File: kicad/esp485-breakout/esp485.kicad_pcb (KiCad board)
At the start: 2 copper layers, 25.4 x 25.4 mm, 21 parts, among them J1 Conn_01x08, J2 Conn_01x08, SW1 SW_Push, SW2 SW_Push, U1 MAX3485, U2 ESP-WROOM-02, U3 AMS1117-3.3

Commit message: font size adjusted
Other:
- board text added: "."
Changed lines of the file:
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@@
   (general
     (thickness 1.6)
-    (drawings 26)
+    (drawings 27)
     (tracks 182)
     (zones 0)
@@
   (layers
     (0 F.Cu signal hide)
-    (31 B.Cu signal)
+    (31 B.Cu signal hide)
     (32 B.Adhes user)
     (33 F.Adhes user)
@@
     (tags "CMS SOT")
     (attr smd)
-    (fp_text reference U3 (at 0.127 0.381 180) (layer B.SilkS)
+    (fp_text reference U3 (at 2.794 3.175 180) (layer B.SilkS)
       (effects (font (size 1 1) (thickness 0.15)) (justify mirror))
     )
@@
     (tags "resistor handsolder")
     (attr smd)
-    (fp_text reference R2 (at -0.254 -1.143) (layer B.SilkS)
-      (effects (font (size 1 1) (thickness 0.15)) (justify mirror))
+    (fp_text reference R2 (at 0 1.143) (layer B.SilkS)
+      (effects (font (size 0.8 0.8) (thickness 0.14)) (justify mirror))
     )
     (fp_text value 10K (at 0 -1.43) (layer B.Fab)
@@
     (tags "resistor handsolder")
     (attr smd)
-    (fp_text reference R3 (at 0.127 -1.143) (layer B.SilkS)
-      (effects (font (size 1 1) (thickness 0.15)) (justify mirror))
+    (fp_text reference R3 (at 0 1.143) (layer B.SilkS)
+      (effects (font (size 0.8 0.8) (thickness 0.14)) (justify mirror))
     )
     (fp_text value 10K (at 0 -1.43) (layer B.Fab)
@@
     (attr smd)
     (fp_text reference R7 (at 0 1.27) (layer B.SilkS)
-      (effects (font (size 1 1) (thickness 0.15)) (justify mirror))
+      (effects (font (size 0.8 0.8) (thickness 0.14)) (justify mirror))
     )
     (fp_text value 10K (at 0 -1.43) (layer B.Fab)
@@
     (attr smd)
     (fp_text reference R8 (at 0 1.016) (layer B.SilkS)
-      (effects (font (size 1 1) (thickness 0.15)) (justify mirror))
+      (effects (font (size 0.8 0.8) (thickness 0.14)) (justify mirror))
     )
     (fp_text value 10K (at 0 -1.43) (layer B.Fab)
@@
     (tags "resistor handsolder")
     (attr smd)
-    (fp_text reference R9 (at -0.381 -1.016) (layer B.SilkS)
-      (effects (font (size 1 1) (thickness 0.15)) (justify mirror))
+    (fp_text reference R9 (at 0 1.143) (layer B.SilkS)
+      (effects (font (size 0.8 0.8) (thickness 0.14)) (justify mirror))
     )
     (fp_text value 10K (at 0 -1.43) (layer B.Fab)
@@
     )
   )
+  (gr_text . (at 145.161 108.839) (layer B.SilkS)
+    (effects (font (size 1.5 1.5) (thickness 0.3)) (justify mirror))
+  )
   (gr_text IO0 (at 131.445 109.22 -90) (layer B.SilkS)

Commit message: esp485-12f added
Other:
- board text added: "+"
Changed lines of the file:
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@@
   (general
     (thickness 1.6)
-    (drawings 27)
+    (drawings 29)
     (tracks 182)
     (zones 0)
@@
     (46 B.CrtYd user)
     (47 F.CrtYd user)
-    (48 B.Fab user hide)
+    (48 B.Fab user)
     (49 F.Fab user)
   )
@@
     (tags "capacitor handsolder")
     (attr smd)
-    (fp_text reference C5 (at -2.54 0 180) (layer B.SilkS)
+    (fp_text reference C5 (at -2.54 0.254 180) (layer B.SilkS)
       (effects (font (size 1 1) (thickness 0.15)) (justify mirror))
     )
@@
     )
   )
+  (gr_text + (at 143.256 98.933) (layer B.SilkS)
+    (effects (font (size 0.8 0.8) (thickness 0.2)) (justify mirror))
+  )
+  (gr_text + (at 143.256 96.266) (layer B.SilkS)
+    (effects (font (size 0.8 0.8) (thickness 0.2)) (justify mirror))
+  )
   (gr_text . (at 145.161 108.839) (layer B.SilkS)

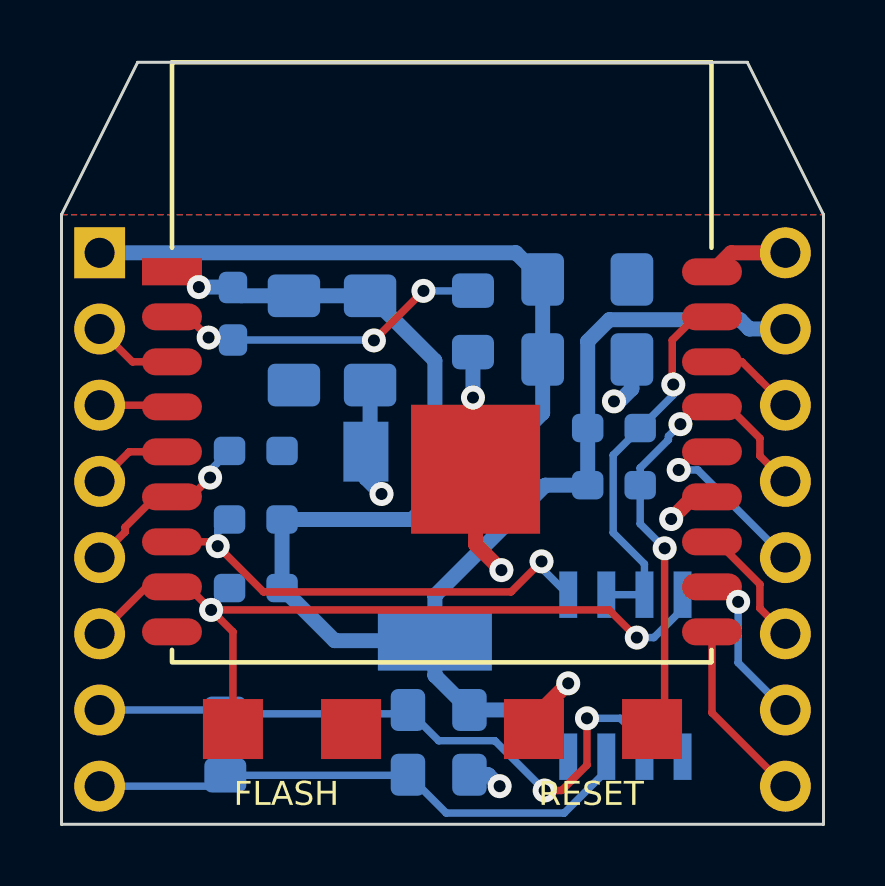
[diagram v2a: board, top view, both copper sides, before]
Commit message: add vias to enlarge gnd pad
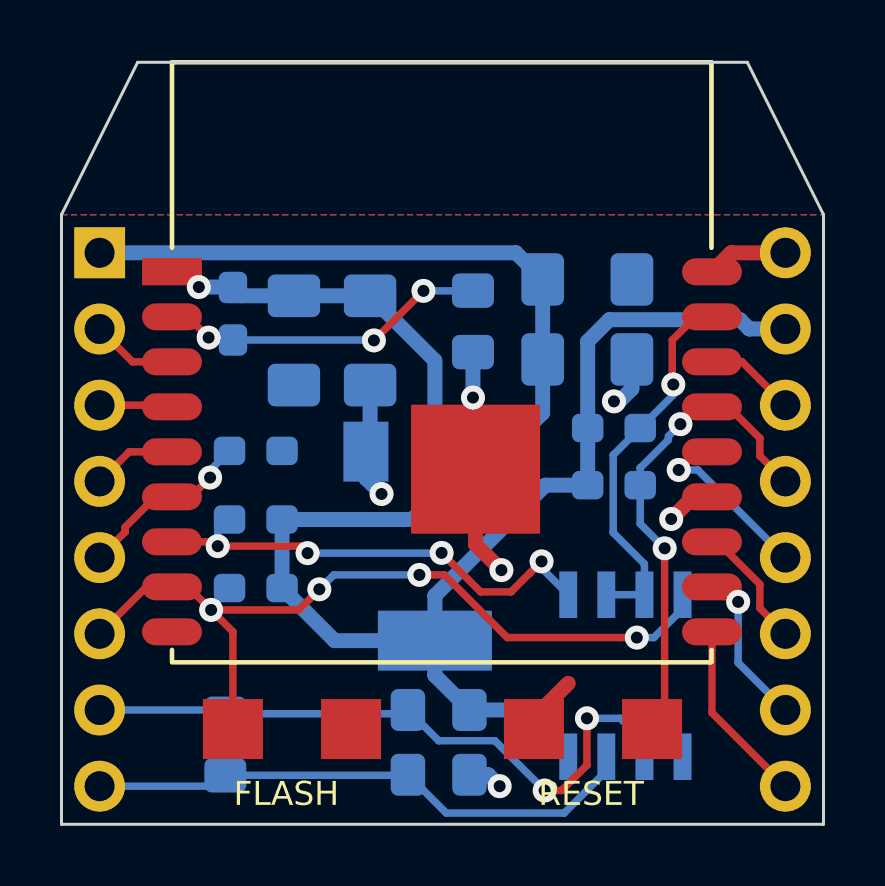
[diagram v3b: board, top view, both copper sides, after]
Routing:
- net Net-(J1-Pad6): track 26.9 -> 27.9 mm, vias 2 -> 4
- net Net-(R2-Pad1): vias 2 -> 4
- net GND: vias 7 -> 6
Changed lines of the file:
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@@
     (thickness 1.6)
     (drawings 29)
-    (tracks 182)
+    (tracks 196)
     (zones 0)
     (modules 21)
@@
   (page A4)
   (layers
-    (0 F.Cu signal hide)
-    (31 B.Cu signal hide)
+    (0 F.Cu signal)
+    (31 B.Cu signal)
     (32 B.Adhes user)
     (33 F.Adhes user)
@@
   (segment (start 133.257414 108.424685) (end 133.257414 108.310586) (width 0.25) (layer B.Cu) (net 2))
   (via (at 147.447 109.347) (size 0.8) (drill 0.4) (layers F.Cu B.Cu) (net 2))
-  (segment (start 133.257414 108.424685) (end 146.524685 108.424685) (width 0.25) (layer F.Cu) (net 2))
-  (segment (start 146.524685 108.424685) (end 147.447 109.347) (width 0.25) (layer F.Cu) (net 2))
+  (segment (start 147.447 109.347) (end 148.016 109.347) (width 0.25) (layer B.Cu) (net 2))
+  (segment (start 148.016 109.347) (end 148.971 108.392) (width 0.25) (layer B.Cu) (net 2) (status 20))
   (segment (start 148.971 108.392) (end 148.971 107.917) (width 0.25) (layer B.Cu) (net 2) (status 30))
-  (segment (start 148.016 109.347) (end 148.971 108.392) (width 0.25) (layer B.Cu) (net 2) (status 20))
-  (segment (start 147.447 109.347) (end 148.016 109.347) (width 0.25) (layer B.Cu) (net 2))
   (segment (start 133.985 109.152271) (end 133.985 112.395) (width 0.25) (layer F.Cu) (net 2) (status 20))
   (segment (start 133.257414 108.424685) (end 133.985 109.152271) (width 0.25) (layer F.Cu) (net 2))
+  (via (at 136.865041 107.736959) (size 0.8) (drill 0.4) (layers F.Cu B.Cu) (net 2))
+  (segment (start 133.257414 108.424685) (end 136.177315 108.424685) (width 0.25) (layer F.Cu) (net 2))
+  (segment (start 136.177315 108.424685) (end 136.865041 107.736959) (width 0.25) (layer F.Cu) (net 2))
+  (via (at 140.199828 107.256976) (size 0.8) (drill 0.4) (layers F.Cu B.Cu) (net 2))
+  (segment (start 136.865041 107.736959) (end 137.345024 107.256976) (width 0.25) (layer B.Cu) (net 2))
+  (segment (start 137.345024 107.256976) (end 140.199828 107.256976) (width 0.25) (layer B.Cu) (net 2))
+  (segment (start 146.881315 109.347) (end 147.447 109.347) (width 0.25) (layer F.Cu) (net 2))
+  (segment (start 143.12759 109.347) (end 146.881315 109.347) (width 0.25) (layer F.Cu) (net 2))
+  (segment (start 141.037566 107.256976) (end 143.12759 109.347) (width 0.25) (layer F.Cu) (net 2))
+  (segment (start 140.199828 107.256976) (end 141.037566 107.256976) (width 0.25) (layer F.Cu) (net 2))
   (segment (start 131.403 104.655) (end 131.953 104.655) (width 0.25) (layer F.Cu) (net 3) (status 30))
   (segment (start 130.389999 105.668001) (end 131.403 104.655) (width 0.25) (layer F.Cu) (net 3) (status 20))
@@
   (segment (start 149.953 104.655) (end 149.333162 104.655) (width 0.5) (layer F.Cu) (net 6) (status 30))
   (segment (start 149.333162 104.655) (end 148.593404 105.394758) (width 0.5) (layer F.Cu) (net 6) (status 10))
-  (via (at 141.986 101.346) (size 0.8) (drill 0.4) (layers F.Cu B.Cu) (net 6))
   (segment (start 141.986 99.831) (end 141.986 101.346) (width 0.5) (layer B.Cu) (net 6) (status 10))
   (segment (start 138.557 103.008) (end 138.416 103.149) (width 0.5) (layer B.Cu) (net 6) (status 30))
   (segment (start 138.557 100.9285) (end 138.557 103.008) (width 0.5) (layer B.Cu) (net 6) (status 30))
-  (via (at 138.938 104.56) (size 0.8) (drill 0.4) (layers F.Cu B.Cu) (net 6))
   (segment (start 138.416 103.149) (end 138.416 104.038) (width 0.5) (layer B.Cu) (net 6) (status 30))
   (segment (start 138.416 104.038) (end 138.938 104.56) (width 0.5) (layer B.Cu) (net 6) (status 10))
-  (via (at 142.875 114.3) (size 0.8) (drill 0.4) (layers F.Cu B.Cu) (net 6))
   (segment (start 141.868 113.919) (end 142.494 113.919) (width 0.5) (layer B.Cu) (net 6) (status 10))
   (segment (start 142.494 113.919) (end 142.875 114.3) (width 0.5) (layer B.Cu) (net 6))
-  (via (at 145.161 110.871) (size 0.8) (drill 0.4) (layers F.Cu B.Cu) (net 6))
   (segment (start 144.018 112.395) (end 144.018 112.014) (width 0.5) (layer F.Cu) (net 6) (status 30))
   (segment (start 144.018 112.014) (end 145.161 110.871) (width 0.5) (layer F.Cu) (net 6) (status 10))
@@
   (segment (start 147.2835 101.051) (end 146.8615 101.473) (width 0.5) (layer B.Cu) (net 6))
   (segment (start 146.8615 101.473) (end 146.685 101.473) (width 0.5) (layer B.Cu) (net 6))
+  (segment (start 147.2835 100.076) (end 147.2835 101.051) (width 0.5) (layer B.Cu) (net 6) (status 10))
+  (via (at 138.938 104.56) (size 0.8) (drill 0.4) (layers F.Cu B.Cu) (net 6))
+  (via (at 141.986 101.346) (size 0.8) (drill 0.4) (layers F.Cu B.Cu) (net 6))
   (via (at 146.685 101.473) (size 0.8) (drill 0.4) (layers F.Cu B.Cu) (net 6))
-  (segment (start 147.2835 100.076) (end 147.2835 101.051) (width 0.5) (layer B.Cu) (net 6) (status 10))
+  (via (at 142.875 114.3) (size 0.8) (drill 0.4) (layers F.Cu B.Cu) (net 6))
   (segment (start 140.716 103.149) (end 140.716 100.1125) (width 0.5) (layer B.Cu) (net 7) (status 10))
   (segment (start 138.557 97.9535) (end 136.017 97.9535) (width 0.5) (layer B.Cu) (net 7) (status 30))
@@
   (segment (start 133.477 106.299) (end 133.477 105.805) (width 0.25) (layer B.Cu) (net 13) (status 20))
   (via (at 144.272 106.807) (size 0.8) (drill 0.4) (layers F.Cu B.Cu) (net 13))
+  (segment (start 144.272 106.807) (end 144.272 107.028) (width 0.25) (layer B.Cu) (net 13))
   (segment (start 144.272 107.028) (end 145.161 107.917) (width 0.25) (layer B.Cu) (net 13) (status 20))
-  (segment (start 144.272 106.807) (end 144.272 107.028) (width 0.25) (layer B.Cu) (net 13))
-  (segment (start 143.256 107.823) (end 144.272 106.807) (width 0.25) (layer F.Cu) (net 13))
-  (segment (start 133.477 106.299) (end 135.001 107.823) (width 0.25) (layer F.Cu) (net 13))
-  (segment (start 135.001 107.823) (end 143.256 107.823) (width 0.25) (layer F.Cu) (net 13))
+  (via (at 136.472 106.531976) (size 0.8) (drill 0.4) (layers F.Cu B.Cu) (net 13))
+  (segment (start 133.477 106.299) (end 136.239024 106.299) (width 0.25) (layer F.Cu) (net 13))
+  (segment (start 136.239024 106.299) (end 136.472 106.531976) (width 0.25) (layer F.Cu) (net 13))
+  (via (at 140.939959 106.522959) (size 0.8) (drill 0.4) (layers F.Cu B.Cu) (net 13))
+  (segment (start 136.472 106.531976) (end 140.930942 106.531976) (width 0.25) (layer B.Cu) (net 13))
+  (segment (start 140.930942 106.531976) (end 140.939959 106.522959) (width 0.25) (layer B.Cu) (net 13))
+  (segment (start 143.872001 107.206999) (end 144.272 106.807) (width 0.25) (layer F.Cu) (net 13))
+  (segment (start 142.240001 107.823001) (end 143.255999 107.823001) (width 0.25) (layer F.Cu) (net 13))
+  (segment (start 143.255999 107.823001) (end 143.872001 107.206999) (width 0.25) (layer F.Cu) (net 13))
+  (segment (start 140.939959 106.522959) (end 142.240001 107.823001) (width 0.25) (layer F.Cu) (net 13))
   (segment (start 130.635 100.155) (end 131.953 100.155) (width 0.25) (layer F.Cu) (net 14) (status 20))
   (segment (start 129.54 99.06) (end 130.635 100.155) (width 0.25) (layer F.Cu) (net 14) (status 10))

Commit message: migrated to single wire half duplex method
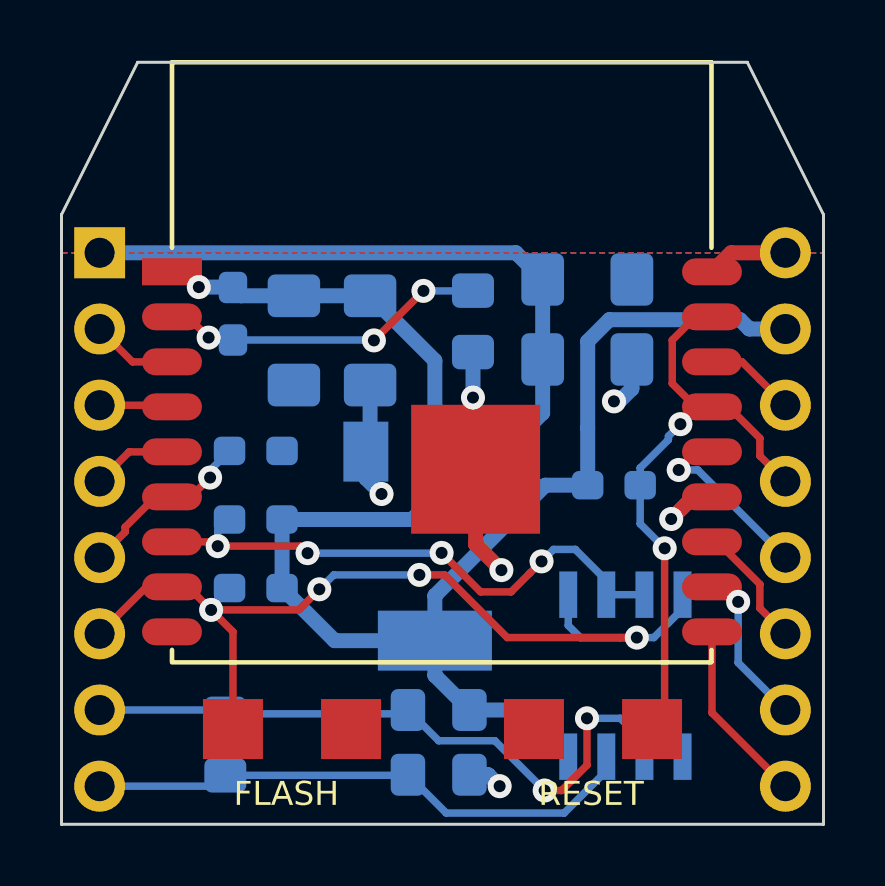
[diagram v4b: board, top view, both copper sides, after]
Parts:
- removed R8: 10K, Resistor_SMD:R_0603_1608Metric_Pad1.05x0.95mm_HandSolder
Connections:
- net Net-(J1-Pad2) renamed /IO14
- net Net-(J1-Pad3) renamed /IO12
- net Net-(J1-Pad4) renamed /IO13
- net Net-(J1-Pad5) renamed /IO15
- net Net-(J1-Pad7) renamed /A
- net Net-(J1-Pad8) renamed /B
- net Net-(J2-Pad3) renamed /TOUT
- net Net-(J2-Pad5) renamed /IO5
- net Net-(J2-Pad6) renamed /TXD
- net Net-(J2-Pad7) renamed /RXD
- net Net-(J2-Pad8) renamed /IO4
- J1 pad 6: Net-(J1-Pad6) -> /IO0
- J2 pad 4: Net-(J2-Pad4) -> /RST
- R3 pad 1: Net-(J1-Pad6) -> /IO0
- R7 pad 2: Net-(J2-Pad4) -> /RST
- SW1 pad 1: Net-(J1-Pad6) -> /IO0
- SW2 pad 1: Net-(J2-Pad4) -> /RST
- U1 pad 1: Net-(R2-Pad1) -> /IO0
- U1 pad 2: Net-(R8-Pad2) -> Net-(R2-Pad1)
- U1 pad 3: Net-(R8-Pad2) -> Net-(R2-Pad1)
- U1 pad 4: Net-(J1-Pad6) -> /IO0
- U2 pad 15: Net-(J2-Pad4) -> /RST
- U2 pad 17: Net-(R8-Pad2) -> /RST
- U2 pad 8: Net-(J1-Pad6) -> /IO0
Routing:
- net /IO0: track 0.00 -> 31.4 mm, vias 0 -> 4
- net Net-(J1-Pad6): track 27.9 -> 0.00 mm, vias 4 -> 0
- net /RST: track 0.00 -> 21.1 mm, vias 0 -> 2
- net Net-(J2-Pad4): track 16.3 -> 0.00 mm, vias 2 -> 0
- net Net-(R8-Pad2): track 12.7 -> 0.00 mm, vias 1 -> 0
- net Net-(R2-Pad1): track 16.0 -> 19.2 mm
- net GND: track 18.4 -> 16.8 mm

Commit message: added 4 layers pcb
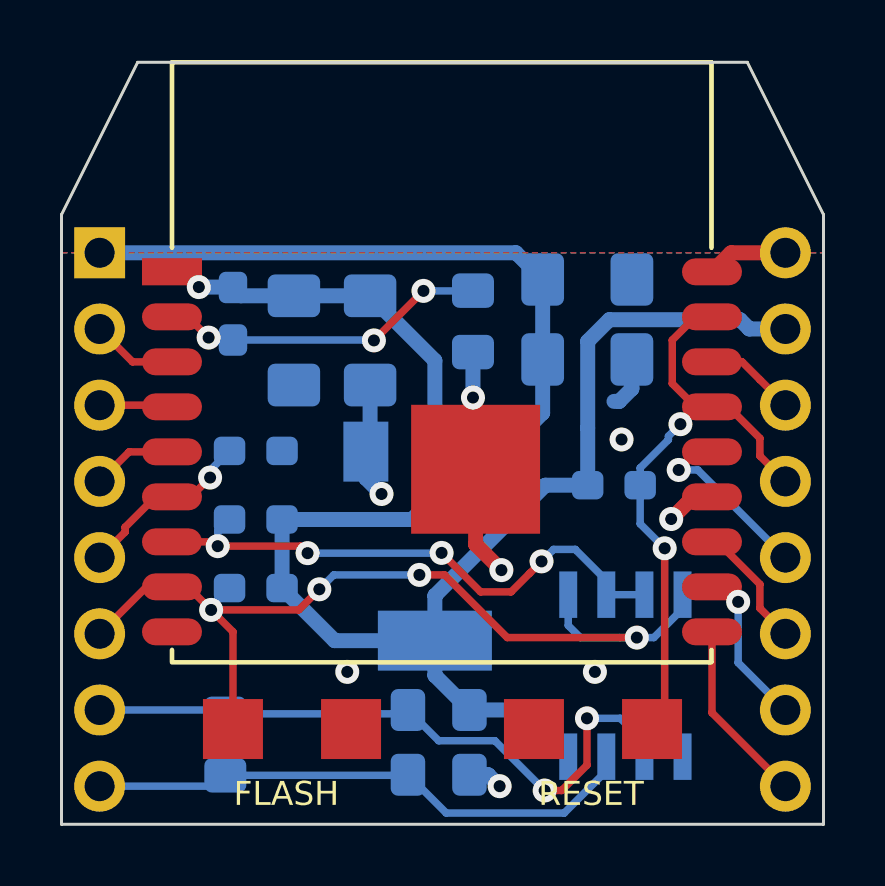
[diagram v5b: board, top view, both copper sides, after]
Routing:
- net GND: vias 6 -> 8

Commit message: put resistor between IO16 and RESET
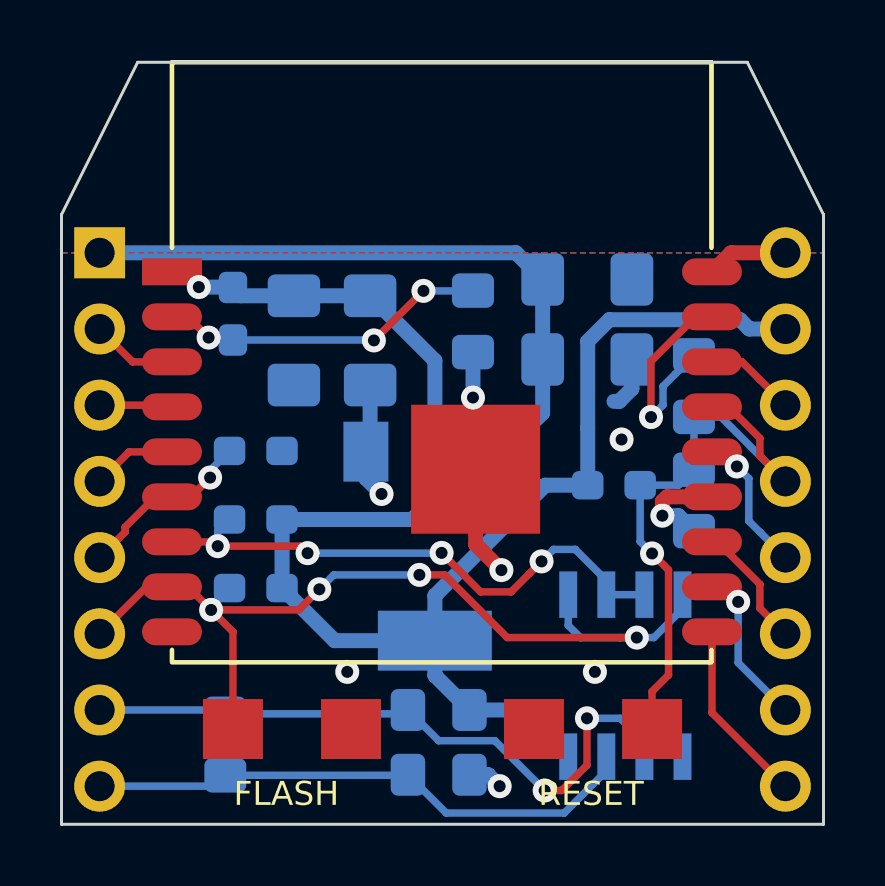
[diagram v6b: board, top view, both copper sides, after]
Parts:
- added C6: C, Capacitor_SMD:C_0805_2012Metric_Pad1.15x1.40mm_HandSolder, B.Cu at (149.4, 104.8)
- added R6: 1k, Resistor_SMD:R_0805_2012Metric_Pad1.15x1.40mm_HandSolder, B.Cu at (149.4, 101.0)
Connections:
- net Net-(C5-Pad1) renamed /EN
- net Net-(R2-Pad1) renamed /IO2
- U2 pad 17: /RST -> /IO16
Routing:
- net /IO16: track 0.00 -> 7.15 mm, vias 0 -> 1
- net GND: track 16.8 -> 18.6 mm
- net /IO5: track 6.13 -> 4.74 mm
- net /RST: track 21.1 -> 20.3 mm, vias 2 -> 1

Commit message: esp485 2layers PCB refined
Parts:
- moved C2 12.2 mm to (133.6, 98.4), turned to 270 degrees
- moved C3 9.85 mm to (148.3, 98.3)
- moved C4 9.72 mm to (145.7, 98.3)
- moved C1 9.67 mm to (136.3, 98.4), turned to 270 degrees
- moved R9 9.37 mm to (143.3, 107.0), turned to 90 degrees
- moved C5 8.66 mm to (134.0, 102.1), turned to 0 degrees
- moved R1 8.52 mm to (134.4, 107.1), turned to 90 degrees
- moved U3 5.97 mm to (141.0, 100.3), turned to 90 degrees
- moved R3 5.55 mm to (140.3, 107.1), turned to 90 degrees
- moved R6 3.70 mm to (148.0, 104.4), turned to 180 degrees
- moved R4 3.66 mm to (137.4, 110.5)
- moved R5 3.45 mm to (137.4, 113.5)
- moved R2 3.05 mm to (137.3, 107.1), turned to 90 degrees
- moved C6 3.01 mm to (148.0, 102.1), turned to 180 degrees
- moved R7 2.85 mm to (146.2, 107.1), turned to 90 degrees
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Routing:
- net /IO15: track 6.04 -> 19.3 mm, vias 1 -> 0
- net GND: track 18.6 -> 10.5 mm, vias 8 -> 4
- net VCC: track 21.4 -> 14.4 mm
- net /A: track 22.1 -> 15.2 mm, vias 2 -> 0
- net /IO2: track 19.2 -> 20.3 mm, vias 4 -> 1
- net /IO0: track 31.4 -> 32.0 mm, vias 4 -> 1
- net /RST: track 20.3 -> 20.9 mm
- net +3V3: track 54.7 -> 54.9 mm, vias 1 -> 3
- net /EN: vias 3 -> 1
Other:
- board text added: "VCC"
- board text removed: "."
- board text removed: "FLASH"
- board text removed: "RESET"
- board text removed: "VIN"
